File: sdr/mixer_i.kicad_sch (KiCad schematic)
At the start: 3 parts, among them Q1 AO3400A, Q2 AO3401A, U6 NC7SVU04P5X

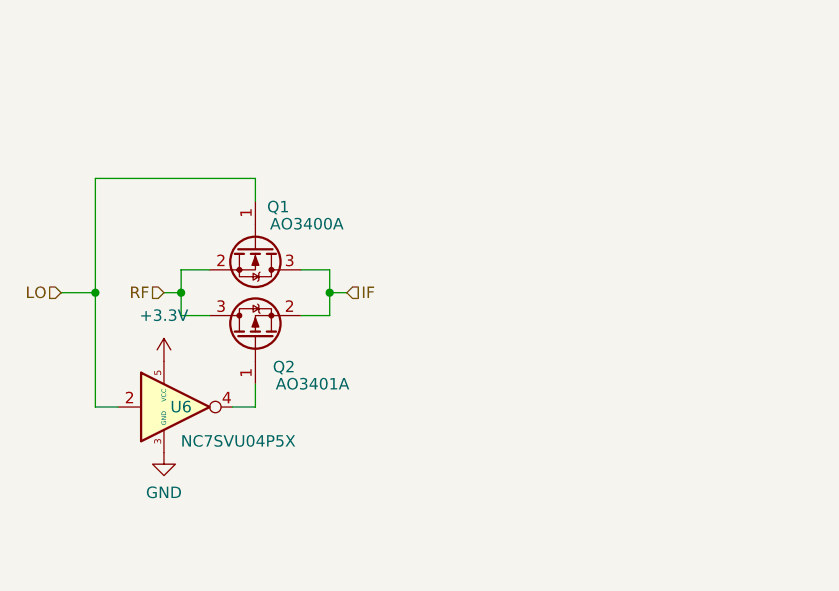
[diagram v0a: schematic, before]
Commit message: Updated the mixer to include some dedicated switches (Gainsail goes to 300 MHz)
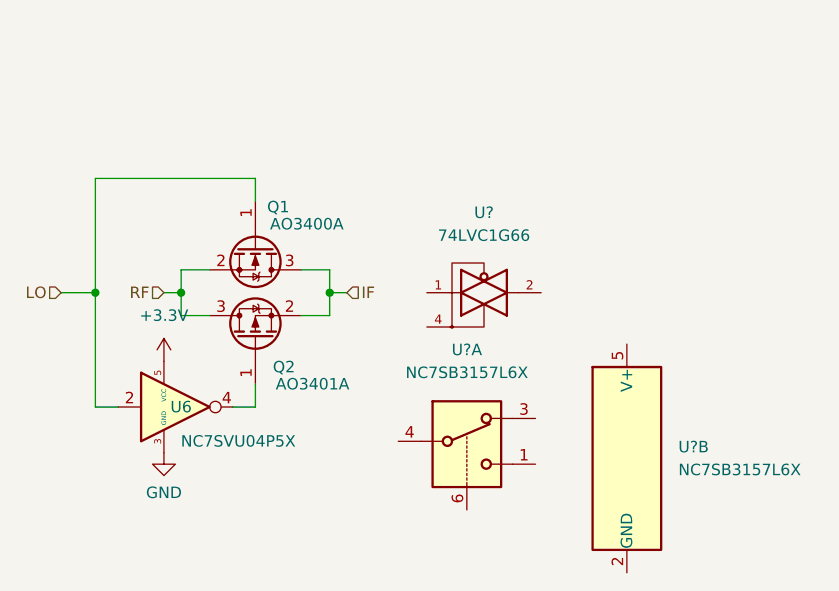
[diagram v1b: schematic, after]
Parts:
- added U? (x2): NC7SB3157L6X, Package_SON:Fairchild_MicroPak-6_1.0x1.45mm_P0.5mm, symbol Analog_Switch:NC7SB3157L6X
- added U?: 74LVC1G66, symbol 74xGxx:74LVC1G66
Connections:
- net GND: now also U?.3 (GND)
- new net VCC: U?.5 (VCC)
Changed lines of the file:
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@@
     (effects (font (size 1.27 1.27)) (justify left))
+  )
+  (symbol (lib_id "Analog_Switch:NC7SB3157L6X") (at 173.355 118.11 0) (unit 1)
+    (in_bom yes) (on_board yes) (fields_autoplaced)
+    (property "Reference" "U?" (id 0) (at 173.355 110.49 0))
+    (property "Value" "NC7SB3157L6X" (id 1) (at 173.355 113.03 0))
+    (property "Footprint" "Package_SON:Fairchild_MicroPak-6_1.0x1.45mm_P0.5mm" (id 2) (at 173.355 125.73 0)
+      (effects (font (size 1.27 1.27)) hide)
+    )
+    (property "Datasheet" "https://www.onsemi.com/pub/Collateral/NC7SB3157-D.PDF" (id 3) (at 173.355 118.11 0)
+      (effects (font (size 1.27 1.27)) hide)
+    )
+    (pin "1")
+    (pin "3")
+    (pin "4")
+    (pin "6")
+    (pin "2")
+    (pin "5")
   )
   (symbol (lib_id "74xGxx:NC7SVU04P5X") (at 139.7 116.84 0) (unit 1)
@@
     )
     (pin "1")
+  )
+  (symbol (lib_id "74xGxx:74LVC1G66") (at 175.26 104.14 0) (unit 1)
+    (in_bom yes) (on_board yes) (fields_autoplaced)
+    (property "Reference" "U?" (id 0) (at 175.26 95.25 0))
+    (property "Value" "74LVC1G66" (id 1) (at 175.26 97.79 0))
+    (property "Footprint" "" (id 2) (at 175.26 104.14 0)
+      (effects (font (size 1.27 1.27)) hide)
+    )
+    (property "Datasheet" "http://www.ti.com/lit/ds/symlink/sn74lvc1g66.pdf" (id 3) (at 175.26 104.14 0)
+      (effects (font (size 1.27 1.27)) hide)
+    )
+    (pin "1")
+    (pin "2")
+    (pin "3")
+    (pin "4")
+    (pin "5")
   )
   (symbol (lib_id "power:GND") (at 139.7 121.92 0) (unit 1)
@@
     (pin "3")
   )
+  (symbol (lib_id "Analog_Switch:NC7SB3157L6X") (at 191.135 122.555 0) (unit 2)
+    (in_bom yes) (on_board yes) (fields_autoplaced)
+    (property "Reference" "U?" (id 0) (at 196.85 121.2849 0)
+      (effects (font (size 1.27 1.27)) (justify left))
+    )
+    (property "Value" "NC7SB3157L6X" (id 1) (at 196.85 123.8249 0)
+      (effects (font (size 1.27 1.27)) (justify left))
+    )
+    (property "Footprint" "Package_SON:Fairchild_MicroPak-6_1.0x1.45mm_P0.5mm" (id 2) (at 191.135 130.175 0)
+      (effects (font (size 1.27 1.27)) hide)
+    )
+    (property "Datasheet" "https://www.onsemi.com/pub/Collateral/NC7SB3157-D.PDF" (id 3) (at 191.135 122.555 0)
+      (effects (font (size 1.27 1.27)) hide)
+    )
+    (pin "1")
+    (pin "3")
+    (pin "4")
+    (pin "6")
+    (pin "2")
+    (pin "5")
+  )
   (symbol (lib_id "Transistor_FET:AO3400A") (at 149.86 99.06 270) (unit 1)

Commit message: Many fixes. Updated mixers to use the analog switches rather than discretes.
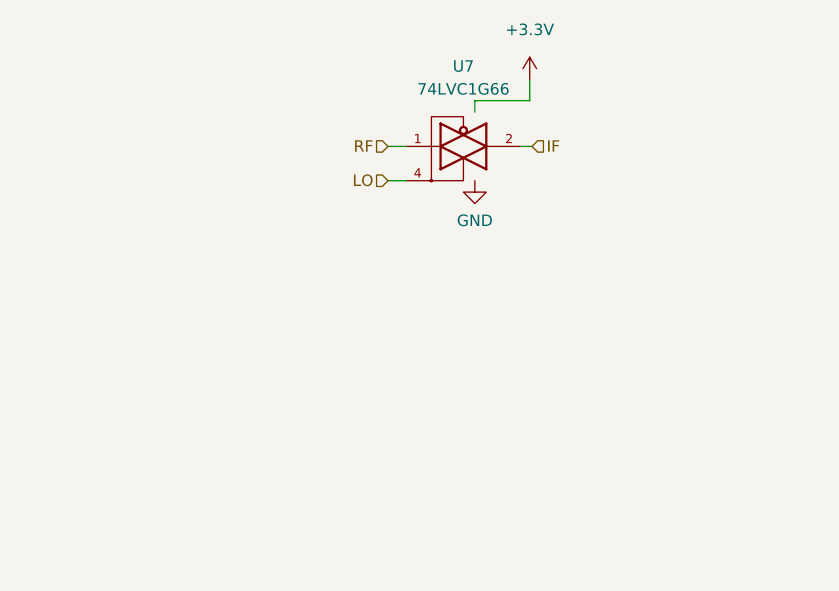
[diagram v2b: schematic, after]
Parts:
- removed Q1: AO3400A, Package_TO_SOT_SMD:SOT-23, symbol Transistor_FET:AO3400A
- removed Q2: AO3401A, Package_TO_SOT_SMD:SOT-23, symbol Transistor_FET:AO3401A
- removed U6: NC7SVU04P5X, Package_TO_SOT_SMD:SOT-353_SC-70-5, symbol 74xGxx:NC7SVU04P5X
- removed U? (x2): NC7SB3157L6X, Package_SON:Fairchild_MicroPak-6_1.0x1.45mm_P0.5mm, symbol Analog_Switch:NC7SB3157L6X
- U7: renamed from U?; footprint (none) -> Package_TO_SOT_SMD:SOT-353_SC-70-5
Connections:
- net VCC is gone; now on net +3.3V: U7.5 (VCC)
- net IF: now also U7.2
- net LO: now also U7.4
- net RF: now also U7.1
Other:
- moved on the sheet: U7
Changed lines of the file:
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@@
 (kicad_sch (version 20211123) (generator eeschema)
   (paper "A4")
-  (junction (at 132.08 104.14) (diameter 0) (color 0 0 0 0)
-  )
-  (junction (at 141.605 104.14) (diameter 0) (color 0 0 0 0)
-  )
-  (junction (at 158.115 104.14) (diameter 0) (color 0 0 0 0)
-  )
-  (wire (pts (xy 128.27 104.14) (xy 132.08 104.14))
+  (wire (pts (xy 180.34 80.518) (xy 180.34 82.804))
     (stroke (width 0) (type default) (color 0 0 0 0))
   )
-  (wire (pts (xy 149.86 114.3) (xy 149.86 116.84))
+  (wire (pts (xy 164.592 87.884) (xy 166.624 87.884))
     (stroke (width 0) (type default) (color 0 0 0 0))
   )
-  (wire (pts (xy 158.115 106.68) (xy 154.94 106.68))
+  (wire (pts (xy 180.34 82.804) (xy 174.244 82.804))
     (stroke (width 0) (type default) (color 0 0 0 0))
   )
-  (wire (pts (xy 132.08 91.44) (xy 149.86 91.44))
+  (wire (pts (xy 164.592 91.694) (xy 166.624 91.694))
     (stroke (width 0) (type default) (color 0 0 0 0))
   )
-  (wire (pts (xy 139.7 104.14) (xy 141.605 104.14))
+  (wire (pts (xy 179.324 87.884) (xy 180.594 87.884))
     (stroke (width 0) (type default) (color 0 0 0 0))
   )
-  (wire (pts (xy 149.86 116.84) (xy 147.32 116.84))
+  (wire (pts (xy 174.244 82.804) (xy 174.244 84.074))
     (stroke (width 0) (type default) (color 0 0 0 0))
   )
-  (wire (pts (xy 141.605 106.68) (xy 144.78 106.68))
-    (stroke (width 0) (type default) (color 0 0 0 0))
-  )
-  (wire (pts (xy 134.62 116.84) (xy 132.08 116.84))
-    (stroke (width 0) (type default) (color 0 0 0 0))
-  )
-  (wire (pts (xy 141.605 101.6) (xy 141.605 104.14))
-    (stroke (width 0) (type default) (color 0 0 0 0))
-  )
-  (wire (pts (xy 158.115 104.14) (xy 160.02 104.14))
-    (stroke (width 0) (type default) (color 0 0 0 0))
-  )
-  (wire (pts (xy 158.115 104.14) (xy 158.115 106.68))
-    (stroke (width 0) (type default) (color 0 0 0 0))
-  )
-  (wire (pts (xy 132.08 104.14) (xy 132.08 91.44))
-    (stroke (width 0) (type default) (color 0 0 0 0))
-  )
-  (wire (pts (xy 144.78 101.6) (xy 141.605 101.6))
-    (stroke (width 0) (type default) (color 0 0 0 0))
-  )
-  (wire (pts (xy 149.86 91.44) (xy 149.86 93.98))
-    (stroke (width 0) (type default) (color 0 0 0 0))
-  )
-  (wire (pts (xy 154.94 101.6) (xy 158.115 101.6))
-    (stroke (width 0) (type default) (color 0 0 0 0))
-  )
-  (wire (pts (xy 141.605 104.14) (xy 141.605 106.68))
-    (stroke (width 0) (type default) (color 0 0 0 0))
-  )
-  (wire (pts (xy 158.115 101.6) (xy 158.115 104.14))
-    (stroke (width 0) (type default) (color 0 0 0 0))
-  )
-  (wire (pts (xy 132.08 116.84) (xy 132.08 104.14))
-    (stroke (width 0) (type default) (color 0 0 0 0))
-  )
-  (hierarchical_label "LO" (shape input) (at 128.27 104.14 180)
+  (hierarchical_label "LO" (shape input) (at 164.592 91.694 180)
     (effects (font (size 1.27 1.27)) (justify right))
   )
-  (hierarchical_label "RF" (shape input) (at 139.7 104.14 180)
+  (hierarchical_label "RF" (shape input) (at 164.592 87.884 180)
     (effects (font (size 1.27 1.27)) (justify right))
   )
-  (hierarchical_label "IF" (shape input) (at 160.02 104.14 0)
+  (hierarchical_label "IF" (shape input) (at 180.594 87.884 0)
     (effects (font (size 1.27 1.27)) (justify left))
   )
-  (symbol (lib_id "Analog_Switch:NC7SB3157L6X") (at 173.355 118.11 0) (unit 1)
+  (symbol (lib_id "power:+3.3V") (at 180.34 80.518 0) (unit 1)
     (in_bom yes) (on_board yes) (fields_autoplaced)
-    (property "Reference" "U?" (id 0) (at 173.355 110.49 0))
-    (property "Value" "NC7SB3157L6X" (id 1) (at 173.355 113.03 0))
-    (property "Footprint" "Package_SON:Fairchild_MicroPak-6_1.0x1.45mm_P0.5mm" (id 2) (at 173.355 125.73 0)
+    (property "Reference" "#PWR057" (id 0) (at 180.34 84.328 0)
       (effects (font (size 1.27 1.27)) hide)
     )
-    (property "Datasheet" "https://www.onsemi.com/pub/Collateral/NC7SB3157-D.PDF" (id 3) (at 173.355 118.11 0)
+    (property "Value" "+3.3V" (id 1) (at 180.34 74.93 0))
+    (property "Footprint" "" (id 2) (at 180.34 80.518 0)
+      (effects (font (size 1.27 1.27)) hide)
+    )
+    (property "Datasheet" "" (id 3) (at 180.34 80.518 0)
       (effects (font (size 1.27 1.27)) hide)
     )
     (pin "1")
-    (pin "3")
-    (pin "4")
-    (pin "6")
-    (pin "2")
-    (pin "5")
   )
-  (symbol (lib_id "74xGxx:NC7SVU04P5X") (at 139.7 116.84 0) (unit 1)
-    (in_bom yes) (on_board yes)
-    (property "Reference" "U6" (id 0) (at 141.605 116.84 0))
-    (property "Value" "NC7SVU04P5X" (id 1) (at 147.955 120.65 0))
-    (property "Footprint" "Package_TO_SOT_SMD:SOT-353_SC-70-5" (id 2) (at 139.7 123.19 0)
+  (symbol (lib_id "74xGxx:74LVC1G66") (at 172.974 87.884 0) (unit 1)
+    (in_bom yes) (on_board yes) (fields_autoplaced)
+    (property "Reference" "U7" (id 0) (at 172.974 78.994 0))
+    (property "Value" "74LVC1G66" (id 1) (at 172.974 81.534 0))
+    (property "Footprint" "Package_TO_SOT_SMD:SOT-353_SC-70-5" (id 2) (at 172.974 87.884 0)
       (effects (font (size 1.27 1.27)) hide)
     )
-    (property "Datasheet" "https://www.onsemi.com/pub/Collateral/NC7SVU04-D.pdf" (id 3) (at 139.7 116.84 0)
+    (property "Datasheet" "http://www.ti.com/lit/ds/symlink/sn74lvc1g66.pdf" (id 3) (at 172.974 87.884 0)
       (effects (font (size 1.27 1.27)) hide)
     )
@@
     (pin "5")
   )
-  (symbol (lib_id "power:+3.3V") (at 139.7 111.76 0) (unit 1)
+  (symbol (lib_id "power:GND") (at 174.244 91.694 0) (unit 1)
     (in_bom yes) (on_board yes) (fields_autoplaced)
-    (property "Reference" "#PWR0107" (id 0) (at 139.7 115.57 0)
+    (property "Reference" "#PWR044" (id 0) (at 174.244 98.044 0)
       (effects (font (size 1.27 1.27)) hide)
     )
-    (property "Value" "+3.3V" (id 1) (at 139.7 106.68 0))
-    (property "Footprint" "" (id 2) (at 139.7 111.76 0)
+    (property "Value" "GND" (id 1) (at 174.244 96.139 0))
+    (property "Footprint" "" (id 2) (at 174.244 91.694 0)
       (effects (font (size 1.27 1.27)) hide)
     )
-    (property "Datasheet" "" (id 3) (at 139.7 111.76 0)
+    (property "Datasheet" "" (id 3) (at 174.244 91.694 0)
       (effects (font (size 1.27 1.27)) hide)
     )
     (pin "1")
   )
-  (symbol (lib_id "74xGxx:74LVC1G66") (at 175.26 104.14 0) (unit 1)
-    (in_bom yes) (on_board yes) (fields_autoplaced)
-    (property "Reference" "U?" (id 0) (at 175.26 95.25 0))
-    (property "Value" "74LVC1G66" (id 1) (at 175.26 97.79 0))
-    (property "Footprint" "" (id 2) (at 175.26 104.14 0)
-      (effects (font (size 1.27 1.27)) hide)
-    )
-    (property "Datasheet" "http://www.ti.com/lit/ds/symlink/sn74lvc1g66.pdf" (id 3) (at 175.26 104.14 0)
-      (effects (font (size 1.27 1.27)) hide)
-    )
-    (pin "1")
-    (pin "2")
-    (pin "3")
-    (pin "4")
-    (pin "5")
-  )
-  (symbol (lib_id "power:GND") (at 139.7 121.92 0) (unit 1)
-    (in_bom yes) (on_board yes) (fields_autoplaced)
-    (property "Reference" "#PWR044" (id 0) (at 139.7 128.27 0)
-      (effects (font (size 1.27 1.27)) hide)
-    )
-    (property "Value" "GND" (id 1) (at 139.7 126.365 0))
-    (property "Footprint" "" (id 2) (at 139.7 121.92 0)
-      (effects (font (size 1.27 1.27)) hide)
-    )
-    (property "Datasheet" "" (id 3) (at 139.7 121.92 0)
-      (effects (font (size 1.27 1.27)) hide)
-    )
-    (pin "1")
-  )
-  (symbol (lib_id "Transistor_FET:AO3401A") (at 149.86 109.22 90) (unit 1)
-    (in_bom yes) (on_board yes)
-    (property "Reference" "Q2" (id 0) (at 153.035 112.395 90))
-    (property "Value" "AO3401A" (id 1) (at 156.21 114.3 90))
-    (property "Footprint" "Package_TO_SOT_SMD:SOT-23" (id 2) (at 151.765 104.14 0)
-      (effects (font (size 1.27 1.27) italic) (justify left) hide)
-    )
-    (property "Datasheet" "http://www.aosmd.com/pdfs/datasheet/AO3401A.pdf" (id 3) (at 149.86 109.22 0)
-      (effects (font (size 1.27 1.27)) (justify left) hide)
-    )
-    (property "LCSC" "C15127" (id 4) (at 153.035 112.395 0)
-      (effects (font (size 1.27 1.27)) hide)
-    )
-    (pin "1")
-    (pin "2")
-    (pin "3")
-  )
-  (symbol (lib_id "Analog_Switch:NC7SB3157L6X") (at 191.135 122.555 0) (unit 2)
-    (in_bom yes) (on_board yes) (fields_autoplaced)
-    (property "Reference" "U?" (id 0) (at 196.85 121.2849 0)
-      (effects (font (size 1.27 1.27)) (justify left))
-    )
-    (property "Value" "NC7SB3157L6X" (id 1) (at 196.85 123.8249 0)
-      (effects (font (size 1.27 1.27)) (justify left))
-    )
-    (property "Footprint" "Package_SON:Fairchild_MicroPak-6_1.0x1.45mm_P0.5mm" (id 2) (at 191.135 130.175 0)
-      (effects (font (size 1.27 1.27)) hide)
-    )
-    (property "Datasheet" "https://www.onsemi.com/pub/Collateral/NC7SB3157-D.PDF" (id 3) (at 191.135 122.555 0)
-      (effects (font (size 1.27 1.27)) hide)
-    )
-    (pin "1")
-    (pin "3")
-    (pin "4")
-    (pin "6")
-    (pin "2")
-    (pin "5")
-  )
-  (symbol (lib_id "Transistor_FET:AO3400A") (at 149.86 99.06 270) (unit 1)
-    (in_bom yes) (on_board yes)
-    (property "Reference" "Q1" (id 0) (at 152.4 94.615 90))
-    (property "Value" "AO3400A" (id 1) (at 155.575 96.52 90))
-    (property "Footprint" "Package_TO_SOT_SMD:SOT-23" (id 2) (at 147.955 104.14 0)
-      (effects (font (size 1.27 1.27) italic) (justify left) hide)
-    )
-    (property "Datasheet" "http://www.aosmd.com/pdfs/datasheet/AO3400A.pdf" (id 3) (at 149.86 99.06 0)
-      (effects (font (size 1.27 1.27)) (justify left) hide)
-    )
-    (property "LCSC" "C20917" (id 4) (at 152.4 94.615 0)
-      (effects (font (size 1.27 1.27)) hide)
-    )
-    (pin "1")
-    (pin "2")
-    (pin "3")
-  )
 )
